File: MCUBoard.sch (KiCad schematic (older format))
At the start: 58 parts, among them J1 USB_B_Micro, J2 Conn_01x04, J3 Conn_02x03_Odd_Even, J4 Conn_02x05_Odd_Even, Q1 BSS138, U1 LM324A, U2 LM324A, U3 STM32F103C8Tx, U4 LT1962-3.3, Y1 8MHz, Y2 32.768KHz

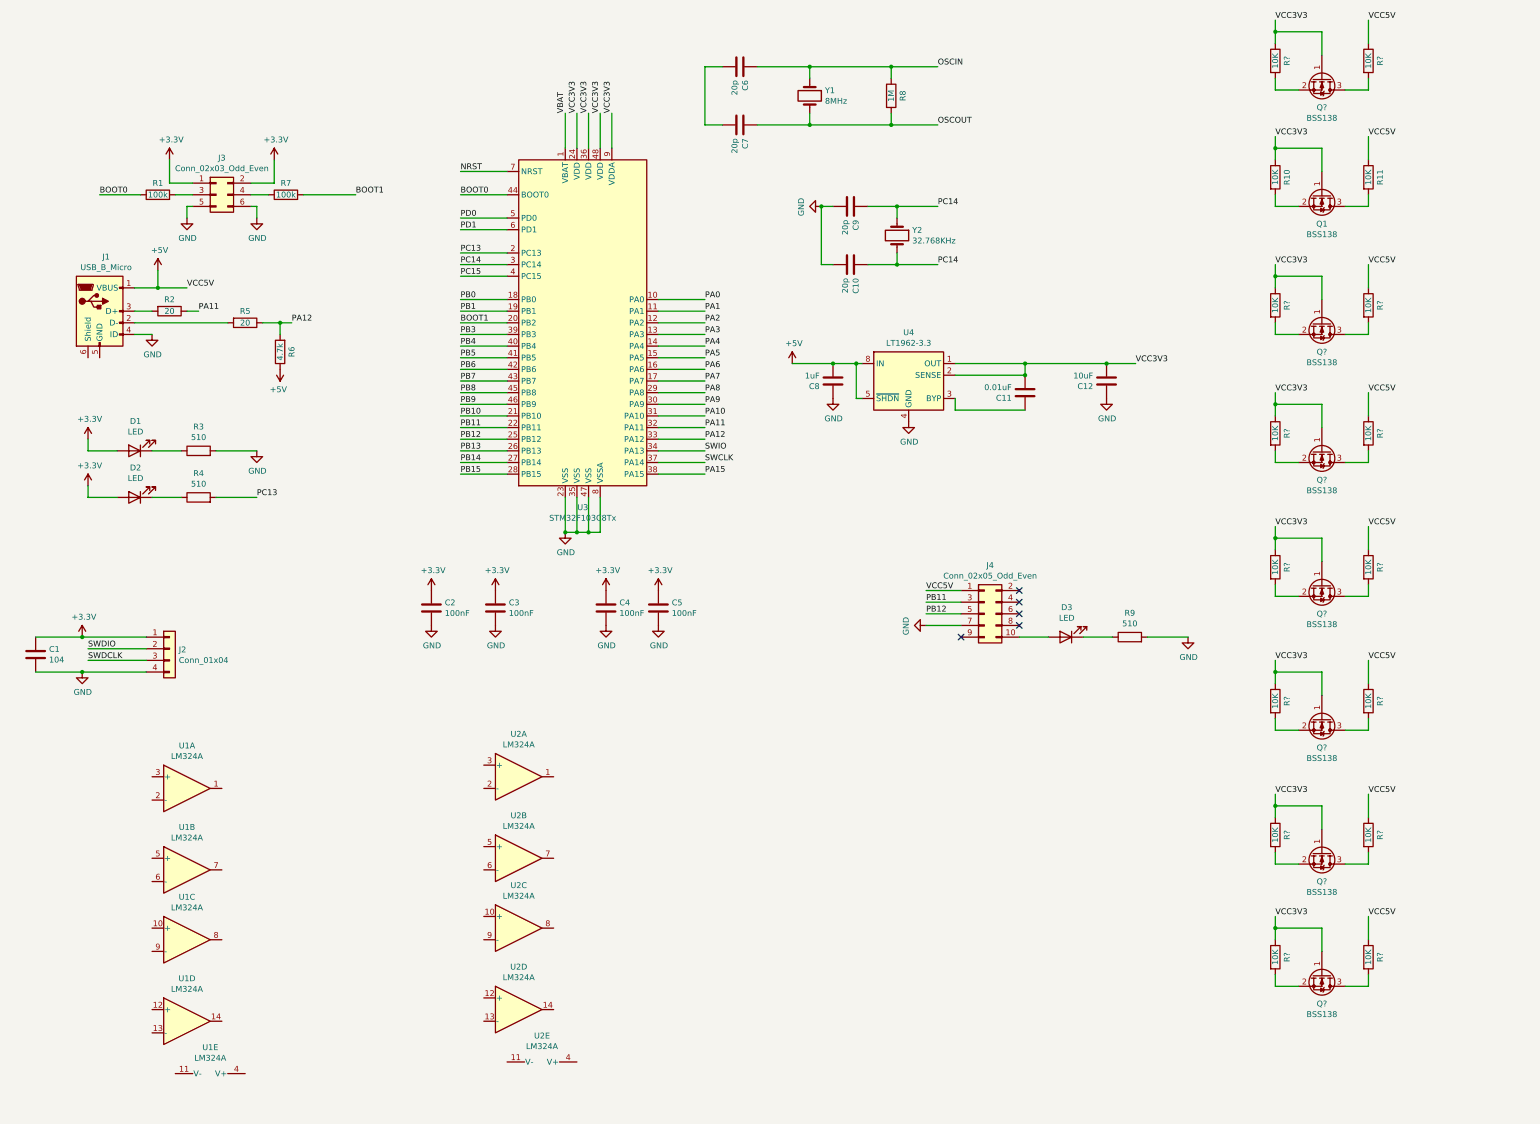
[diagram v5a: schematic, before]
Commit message: add jumpers, non-inverting amps
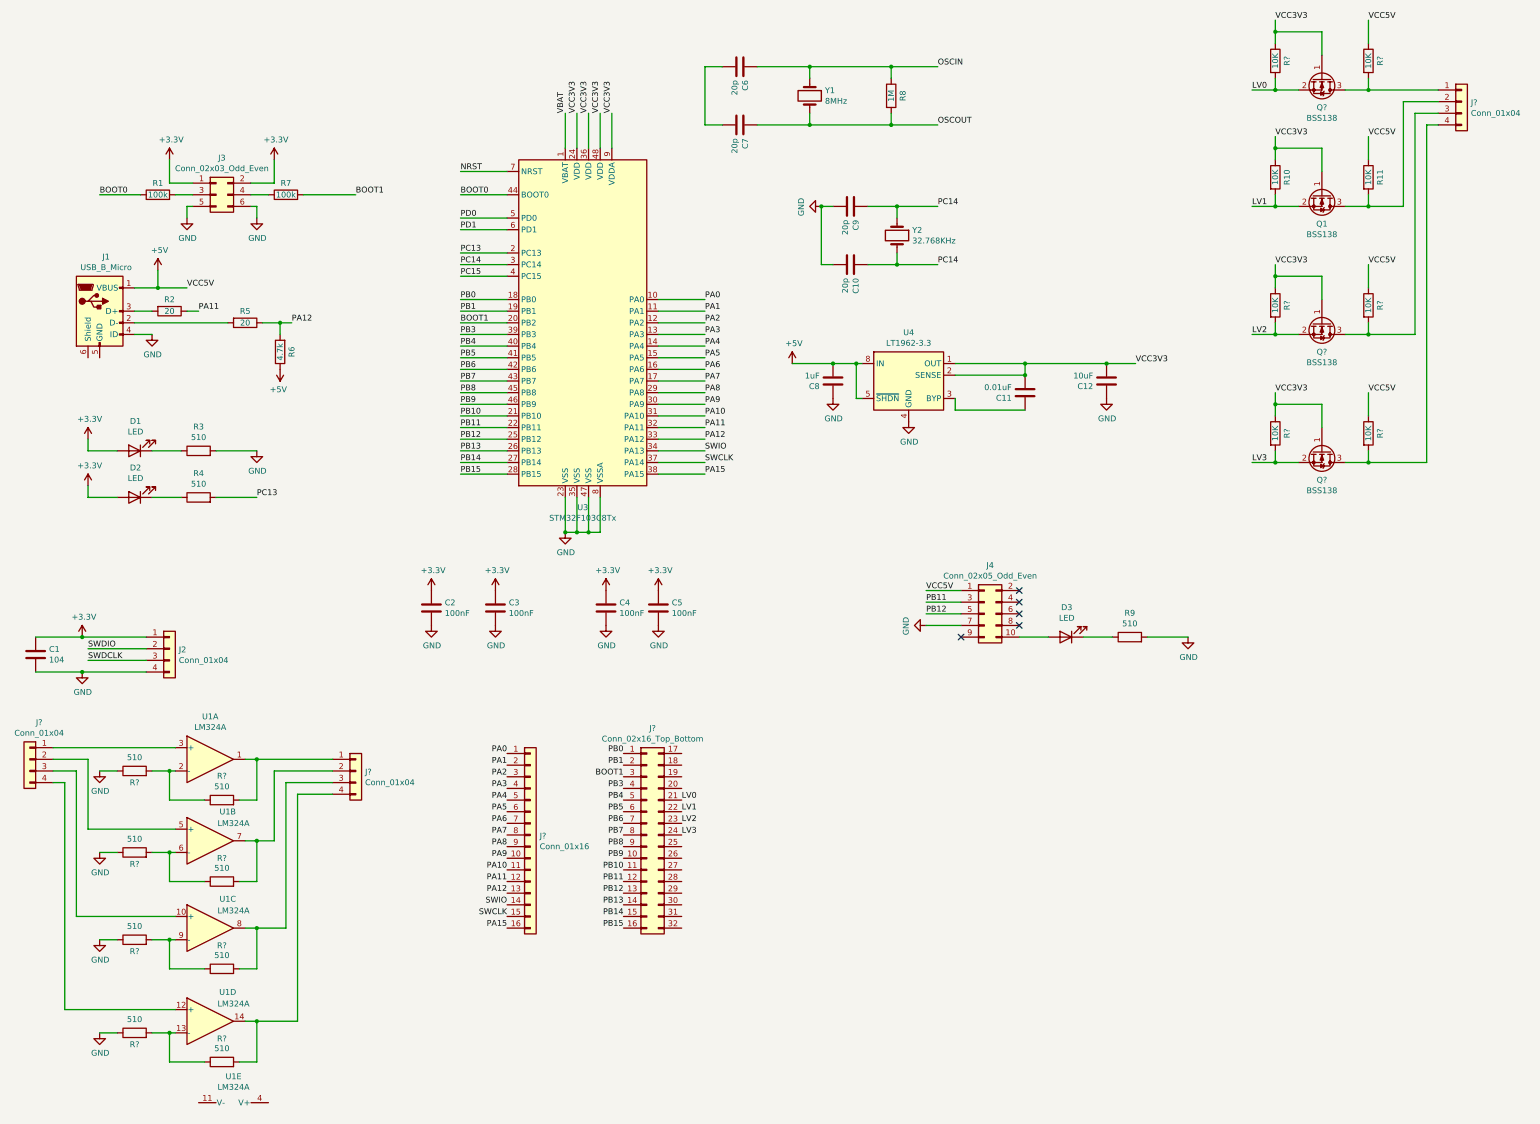
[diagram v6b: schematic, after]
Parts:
- removed Q? (x4): BSS138, Package_TO_SOT_SMD:SOT-23, symbol Transistor_FET:BSS138
- removed R? (x8): 10K, symbol Device:R
- removed U2: LM324A, symbol Amplifier_Operational:LM324A
- added J? (x3): Conn_01x04, symbol Connector_Generic:Conn_01x04
- added J?: Conn_01x16, symbol Connector_Generic:Conn_01x16
- added J?: Conn_02x16_Top_Bottom, symbol Connector_Generic:Conn_02x16_Top_Bottom
- added R? (x8): 510, symbol Device:R
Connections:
- net BOOT1: now also J?.3 (Pin_3)
- net GND: now also R?.1, R?.1, R?.1, R?.1
- net PA0: now also J?.1 (Pin_1)
- net PA1: now also J?.2 (Pin_2)
- net PA10: now also J?.11 (Pin_11)
- net PA11: now also J?.12 (Pin_12)
- net PA12: now also J?.13 (Pin_13)
- net PA15: now also J?.16 (Pin_16)
- net PA2: now also J?.3 (Pin_3)
- net PA3: now also J?.4 (Pin_4)
- net PA4: now also J?.5 (Pin_5)
- net PA5: now also J?.6 (Pin_6)
- net PA6: now also J?.7 (Pin_7)
- net PA7: now also J?.8 (Pin_8)
- net PA8: now also J?.9 (Pin_9)
- net PA9: now also J?.10 (Pin_10)
- net PB0: now also J?.1 (Pin_1)
- net PB1: now also J?.2 (Pin_2)
- net PB10: now also J?.11 (Pin_11)
- net PB11: now also J?.12 (Pin_12)
- net PB12: now also J?.13 (Pin_13)
- net PB13: now also J?.14 (Pin_14)
- net PB14: now also J?.15 (Pin_15)
- net PB15: now also J?.16 (Pin_16)
- net PB3: now also J?.4 (Pin_4)
- net PB4: now also J?.5 (Pin_5)
- net PB5: now also J?.6 (Pin_6)
- net PB6: now also J?.7 (Pin_7)
- net PB7: now also J?.8 (Pin_8)
- net PB8: now also J?.9 (Pin_9)
- net PB9: now also J?.10 (Pin_10)
- net SWCLK: now also J?.15 (Pin_15)
- net SWIO: now also J?.14 (Pin_14)
- net LV1: now reaches Q1.2 (S), R10.2
- net LV1: now also J?.22 (Pin_22)
- net at Q1.3 (D), R11.2: now also J?.2 (Pin_2)
- net at U1.1: now also J?.1 (Pin_1), R?.2
- net at U1.2 (-): now also R?.1, R?.2
- net at U1.3 (+): now also J?.1 (Pin_1)
- net at U1.5 (+): now also J?.2 (Pin_2)
- net at U1.6 (-): now also R?.1, R?.2
- net at U1.7: now also J?.2 (Pin_2), R?.2
- net at U1.10 (+): now also J?.3 (Pin_3)
- net at U1.8: now also J?.3 (Pin_3), R?.2
- net at U1.9 (-): now also R?.1, R?.2
- net at U1.12 (+): now also J?.4 (Pin_4)
- net at U1.13 (-): now also R?.1, R?.2
- net at U1.14: now also J?.4 (Pin_4), R?.2
- net LV0: now reaches Q?.2 (S), R?.2
- net LV0: now also J?.21 (Pin_21)
- net at Q?.3 (D), R?.2: now also J?.1 (Pin_1)
- net LV2: now reaches Q?.2 (S), R?.2
- net LV2: now also J?.23 (Pin_23)
- net at Q?.3 (D), R?.2: now also J?.3 (Pin_3)
- net LV3: now reaches Q?.2 (S), R?.2
- net LV3: now also J?.24 (Pin_24)
- net at Q?.3 (D), R?.2: now also J?.4 (Pin_4)
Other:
- moved on the sheet: U1A, U1B, U1C, U1D, U1E

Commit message: add power flag, removed all ERC warnings/errors
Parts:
- added C13: C, symbol Device:C
- added R26: R, symbol Device:R
- added SW1: SW_Push, symbol Switch:SW_Push
- gave numbers to parts that had none: 22
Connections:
- net SWCLK is gone; now on net SWDCLK: J7.15 (Pin_15), U3.37 (PA14)
- net SWIO is gone; now on net SWDIO: J7.14 (Pin_14), U3.34 (PA13)
- net VBAT is gone; now on net VCC3V3: U3.1 (VBAT)
- net +3V3: now also R26.1
- net +5V: now also U1.4 (V+)
- net GND: now also J1.5 (GND), J1.6 (Shield), U1.11 (V-), C13.2, SW1.1
- net NRST: now also C13.1, R26.2, SW1.2
- net PC14: no longer C10.1, Y2.2
- net PC15: now also C10.1, Y2.2
- net PD0: now also J8.17 (Pin_17)
- net PD1: now also J8.18 (Pin_18)
- no-connect marks 5 -> 16

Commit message: place parts
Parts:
- removed J8: Conn_02x16_Top_Bottom, symbol Connector_Generic:Conn_02x16_Top_Bottom
- added J8: Conn_02x16_Odd_Even, Connector_PinHeader_2.54mm:PinHeader_2x16_P2.54mm_Vertical, symbol Connector_Generic:Conn_02x16_Odd_Even
- C1, C10, C11, C12, C13, C2, C3, C4, C5, C6, C7, C8, C9: footprint (none) -> Capacitor_SMD:C_1806_4516Metric_Pad1.57x1.80mm_HandSolder
- D1, D2, D3: footprint (none) -> LED_SMD:LED_1206_3216Metric_Pad1.42x1.75mm_HandSolder
- J1: footprint (none) -> Connector_USB:USB_Micro-B_Molex_47346-0001
- J2, J5, J6, J9: footprint (none) -> Connector_PinHeader_2.54mm:PinHeader_1x04_P2.54mm_Vertical
- J3: footprint (none) -> Connector_PinHeader_2.54mm:PinHeader_2x03_P2.54mm_Vertical
- J4: footprint (none) -> Connector_PinHeader_2.54mm:PinHeader_2x05_P2.54mm_Vertical
- J7: footprint (none) -> Connector_PinHeader_2.54mm:PinHeader_1x16_P2.54mm_Vertical
- Q1, Q2, Q3, Q4: footprint Package_TO_SOT_SMD:SOT-23 -> Package_TO_SOT_SMD:SOT-23_Handsoldering
- R1, R10, R11, R12, R13, R14, R15, R16, R17, R18, R19, R2, R20, R21, R22, R23, R24, R25, R26, R3, R4, R5, R6, R7, R8, R9: footprint (none) -> Resistor_SMD:R_1806_4516Metric_Pad1.57x1.80mm_HandSolder
- SW1: footprint (none) -> Button_Switch_THT:SW_PUSH_6mm
- U1: footprint (none) -> libs:LM324-SOIC-14
- Y1, Y2: footprint (none) -> Crystal:Crystal_SMD_0603-2Pin_6.0x3.5mm_HandSoldering
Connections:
- net BOOT1: now also J8.5 (Pin_5)
- net LV0: now also J8.10 (Pin_10)
- net LV1: now also J8.12 (Pin_12)
- net LV2: now also J8.14 (Pin_14)
- net LV3: now also J8.16 (Pin_16)
- net PB0: now also J8.1 (Pin_1)
- net PB1: now also J8.3 (Pin_3)
- net PB10: now also J8.21 (Pin_21)
- net PB11: now also J8.23 (Pin_23)
- net PB12: now also J8.25 (Pin_25)
- net PB13: now also J8.27 (Pin_27)
- net PB14: now also J8.29 (Pin_29)
- net PB15: now also J8.31 (Pin_31)
- net PB3: now also J8.7 (Pin_7)
- net PB4: now also J8.9 (Pin_9)
- net PB5: now also J8.11 (Pin_11)
- net PB6: now also J8.13 (Pin_13)
- net PB7: now also J8.15 (Pin_15)
- net PB8: now also J8.17 (Pin_17)
- net PB9: now also J8.19 (Pin_19)
- net PD0: now also J8.2 (Pin_2)
- net PD1: now also J8.4 (Pin_4)
